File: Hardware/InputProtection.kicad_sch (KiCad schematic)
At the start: 7 parts, among them J6 USB_C_Receptacle_USB2.0_14P

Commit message: further clean up, switch to desktop
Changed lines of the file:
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@@
 		(end 193.04 99.06)
 		(stroke
-			(width 0.1778)
+			(width 0.1524)
 			(type solid)
 		)

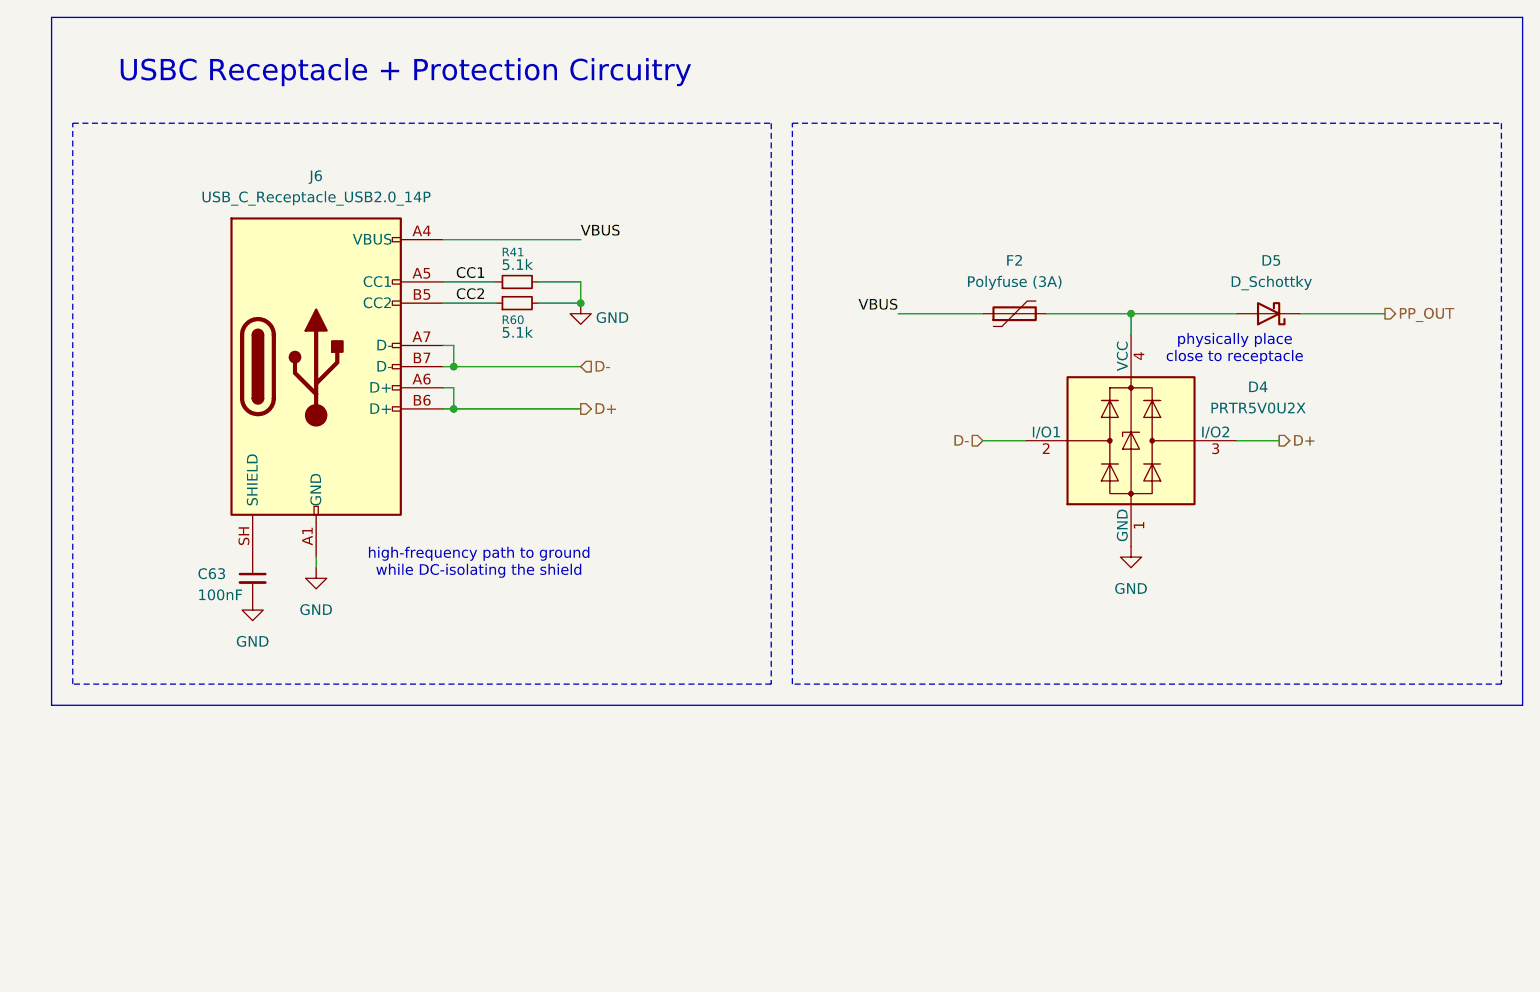
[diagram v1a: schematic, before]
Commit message: new buck ic with 6A current limit, more organization and changes
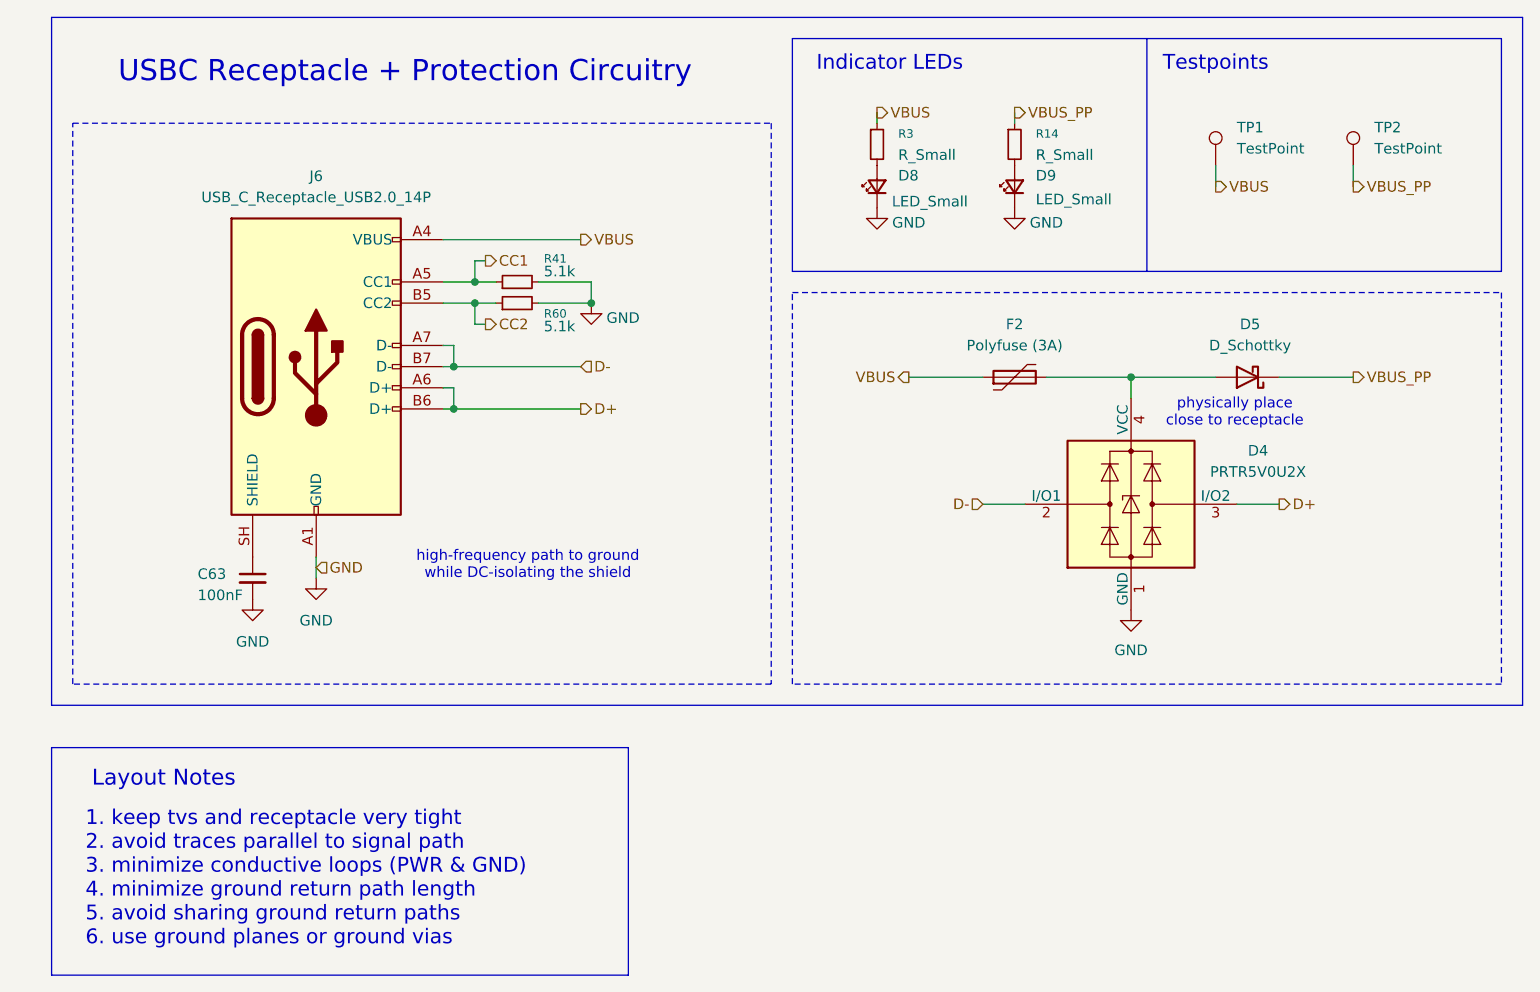
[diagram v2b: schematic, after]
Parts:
- added D8, D9: LED_Small, symbol Device:LED_Small
- added R14, R3: R_Small, symbol Device:R_Small
- added TP1, TP2: TestPoint, symbol Connector:TestPoint
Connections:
- net GND: now also D8.1 (K), D9.1 (K)
- net VBUS: now also R3.1, TP1.1
- net PP_OUT renamed VBUS_PP
- net VBUS_PP: now also R14.1, TP2.1
- new net: D9.2 (A), R14.2
- new net: D8.2 (A), R3.2
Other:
- note added: "1. keep tvs and receptacle very tight 2. avoid traces parallel to signal path 3. minimize conductive loops (PWR & GND) 4. minimize ground return path length 5. avoid sharing ground return paths 6. use ground planes or ground vias"
- note added: "Indicator LEDs"
- note added: "Layout Notes"
- note added: "Testpoints"
- moved on the sheet: D4, D5, F2

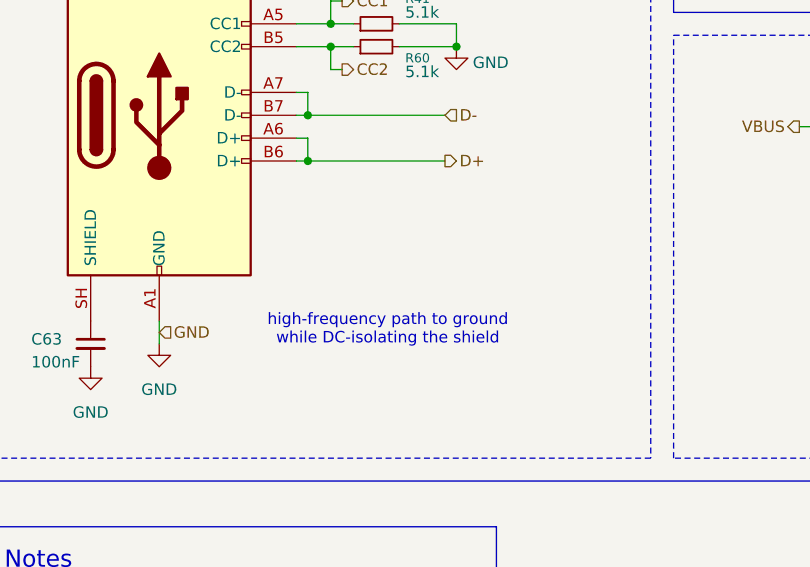
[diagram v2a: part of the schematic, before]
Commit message: added more testpoints and indicator LEDs, added application notes
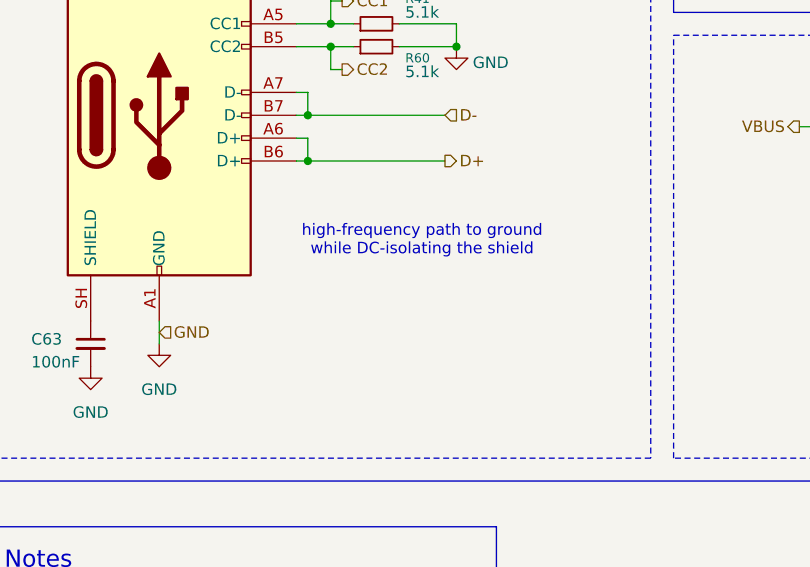
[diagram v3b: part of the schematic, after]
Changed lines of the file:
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@@
 	(text "high-frequency path to ground \nwhile DC-isolating the shield"
 		(exclude_from_sim no)
-		(at 73.66 82.296 0)
+		(at 77.47 72.39 0)
 		(effects
 			(font
